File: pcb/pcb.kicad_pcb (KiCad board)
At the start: 2 copper layers, 50 x 60 mm, 66 parts, among them J1 Battery, J10 Conn_01x04_Male, J11 STM32_SWD, J2 MOTOR_Vcc, J3 MOTOR_5V, J4 MOTOR_OUT, J5 US_SENSOR, J6 BUMPER_SENSOR_FRONT, J7 BUMPER_SENSOR_BACK, J8 BT_USART, J9 GPIO, SW1 SW_Push, U1 LM317_TO-252, U2 L293D, U3 AMS1117-5.0, U4 AMS1117-3.3, U5 STM32F103C8T6, Y1 X322516MLB4SI

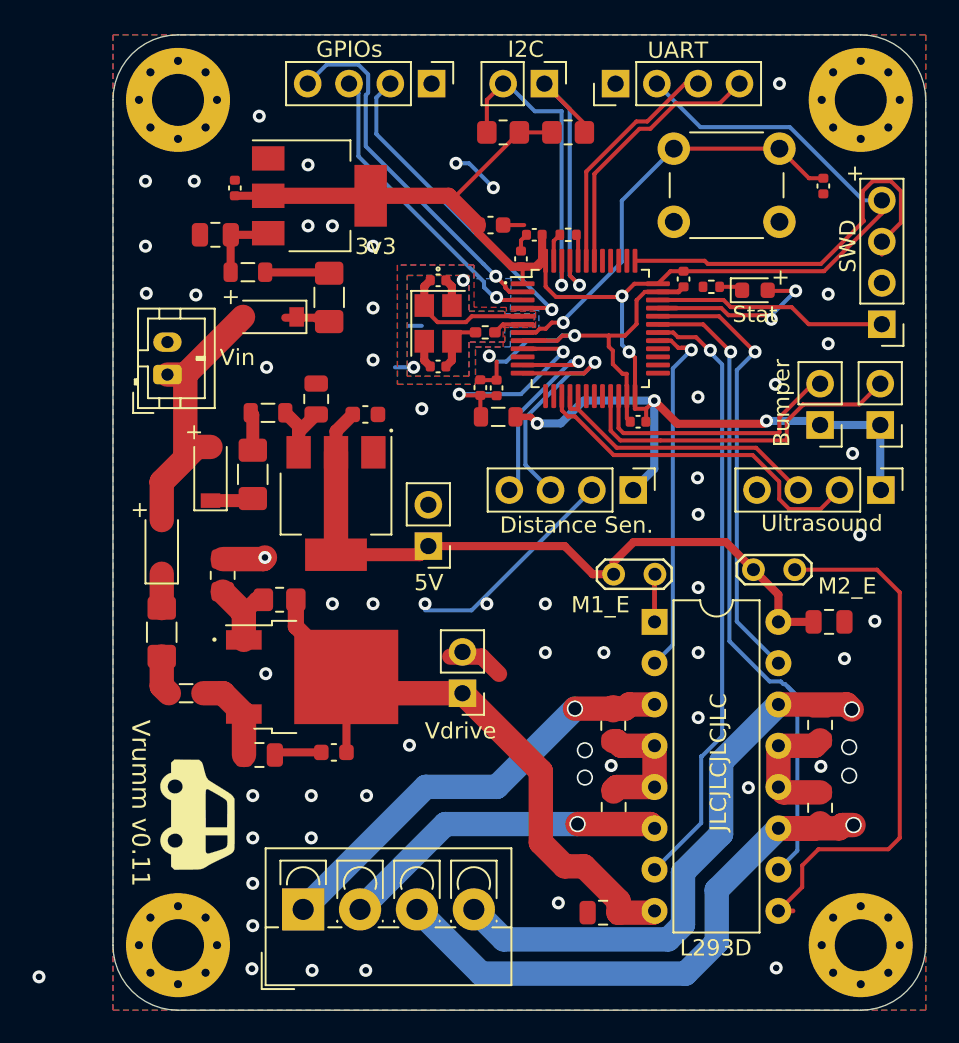
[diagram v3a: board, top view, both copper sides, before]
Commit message: Vcc resistor network reverted, heatsinks to voltage regulators
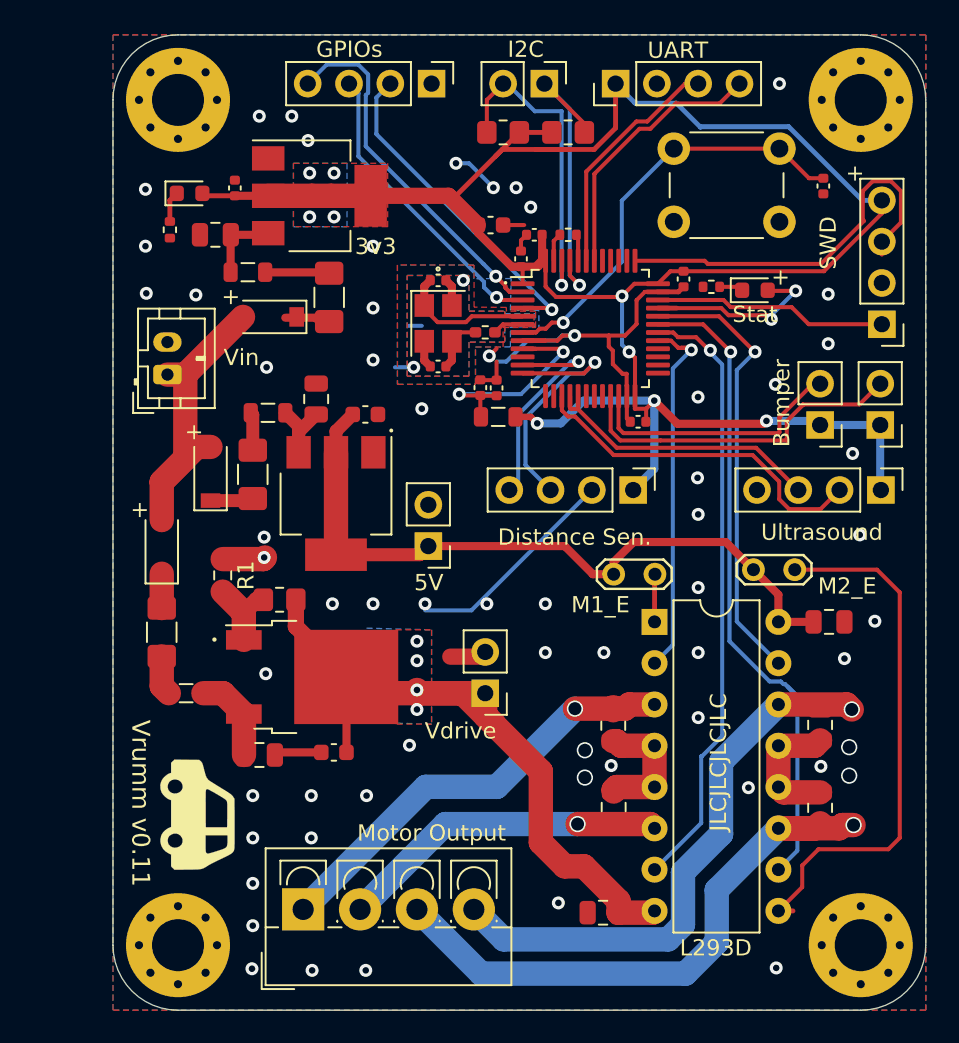
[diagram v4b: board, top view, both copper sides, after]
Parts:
- added D5: Red LED, LED_SMD:LED_0603_1608Metric, F.Cu at (16.7, 21.8)
- added R3: 2k2, Resistor_SMD:R_0402_1005Metric, F.Cu at (15.5, 24.0)
- J1: value Battery -> Battery Input
- J2: value MOTOR_Vcc -> Vdrive output
- J3: value MOTOR_5V -> 5V output
- R1: value 1.5k -> 910; footprint Resistor_SMD:R_0805_2012Metric_Pad1.20x1.40mm_HandSolder -> Resistor_SMD:R_0603_1608Metric_Pad0.98x0.95mm_HandSolder
- moved J2 1.40 mm to (34.9, 52.5)
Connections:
- J8 pad 1: GND -> +3V3
- J8 pad 2: +3V3 -> GND
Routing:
- net +3V3: track 121.0 -> 138.4 mm, vias 5 -> 9
- net Vdrive: track 41.7 -> 49.5 mm, vias 0 -> 4
- net Net-(D5-Pad1): track 0.00 -> 1.91 mm
- net GND: track 77.9 -> 77.1 mm, vias 63 -> 64
- net (no net): vias 1 -> 0
- added copper zone on B.Cu, net +3V3
- added copper zone on F.Cu, net +3V3
- added copper zone on B.Cu, net Vdrive
- added copper zone on F.Cu, net Vdrive
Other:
- board text added: "Motor Output"
- board text removed: "+9.1V"
